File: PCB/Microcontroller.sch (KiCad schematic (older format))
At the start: 5 parts

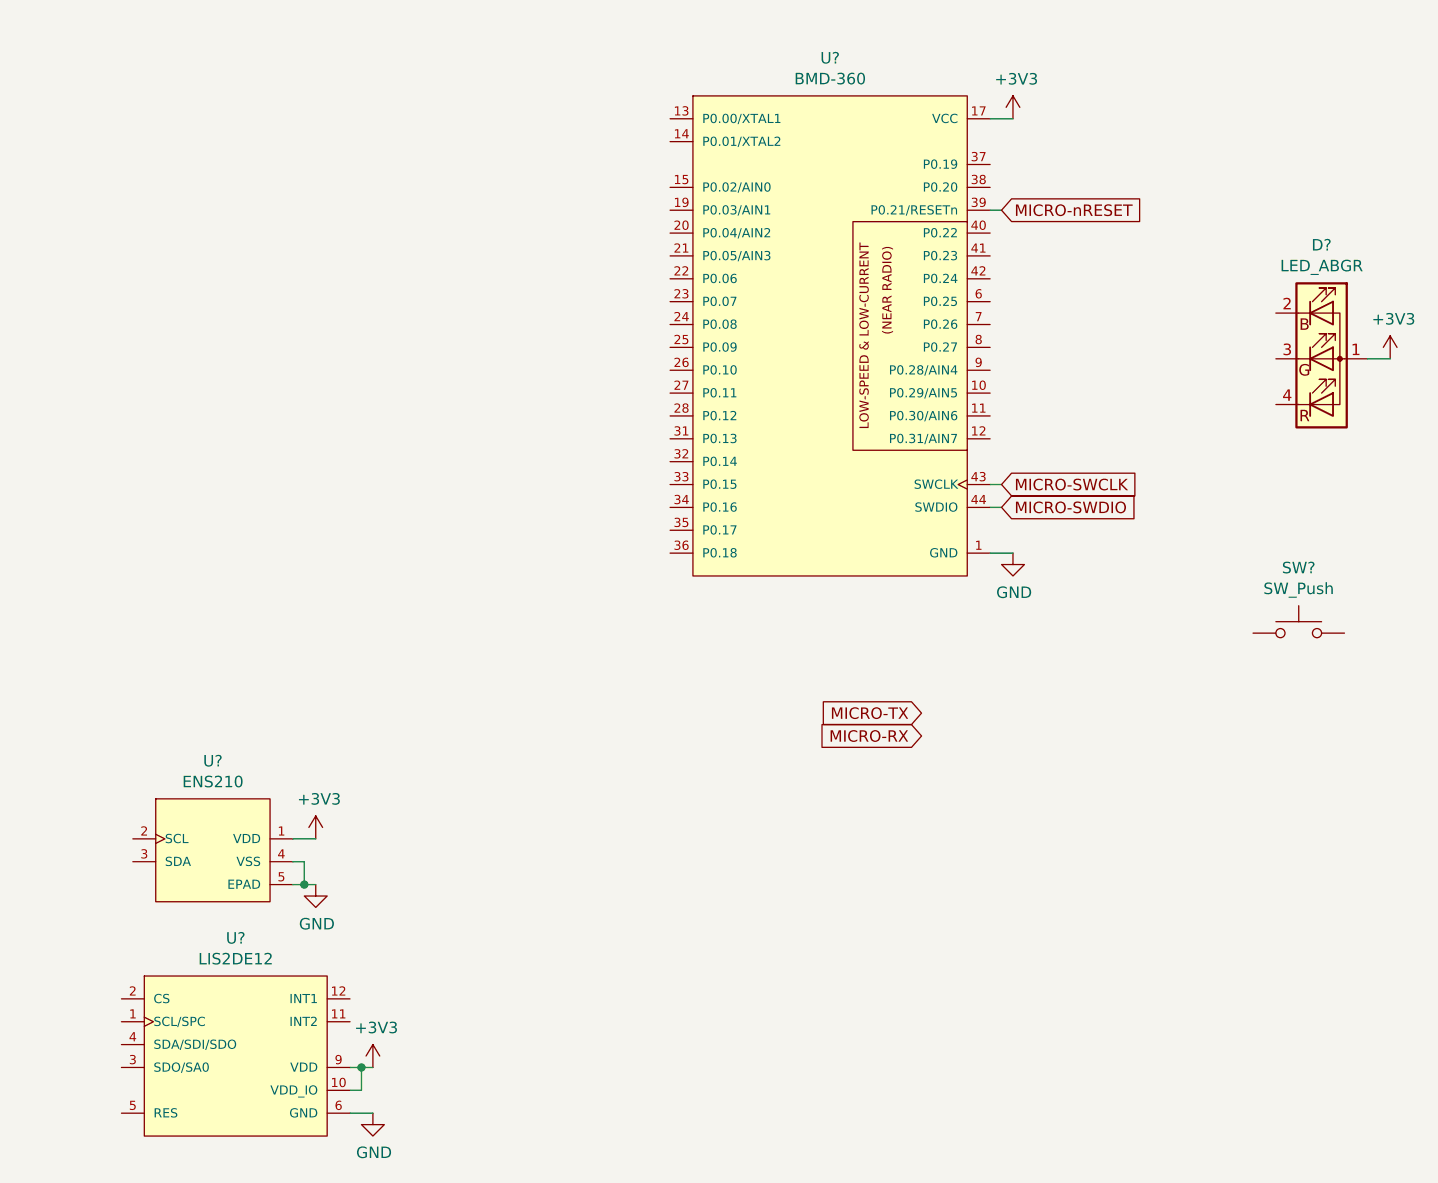
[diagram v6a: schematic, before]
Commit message: Add connections between FPGA and microcontroller
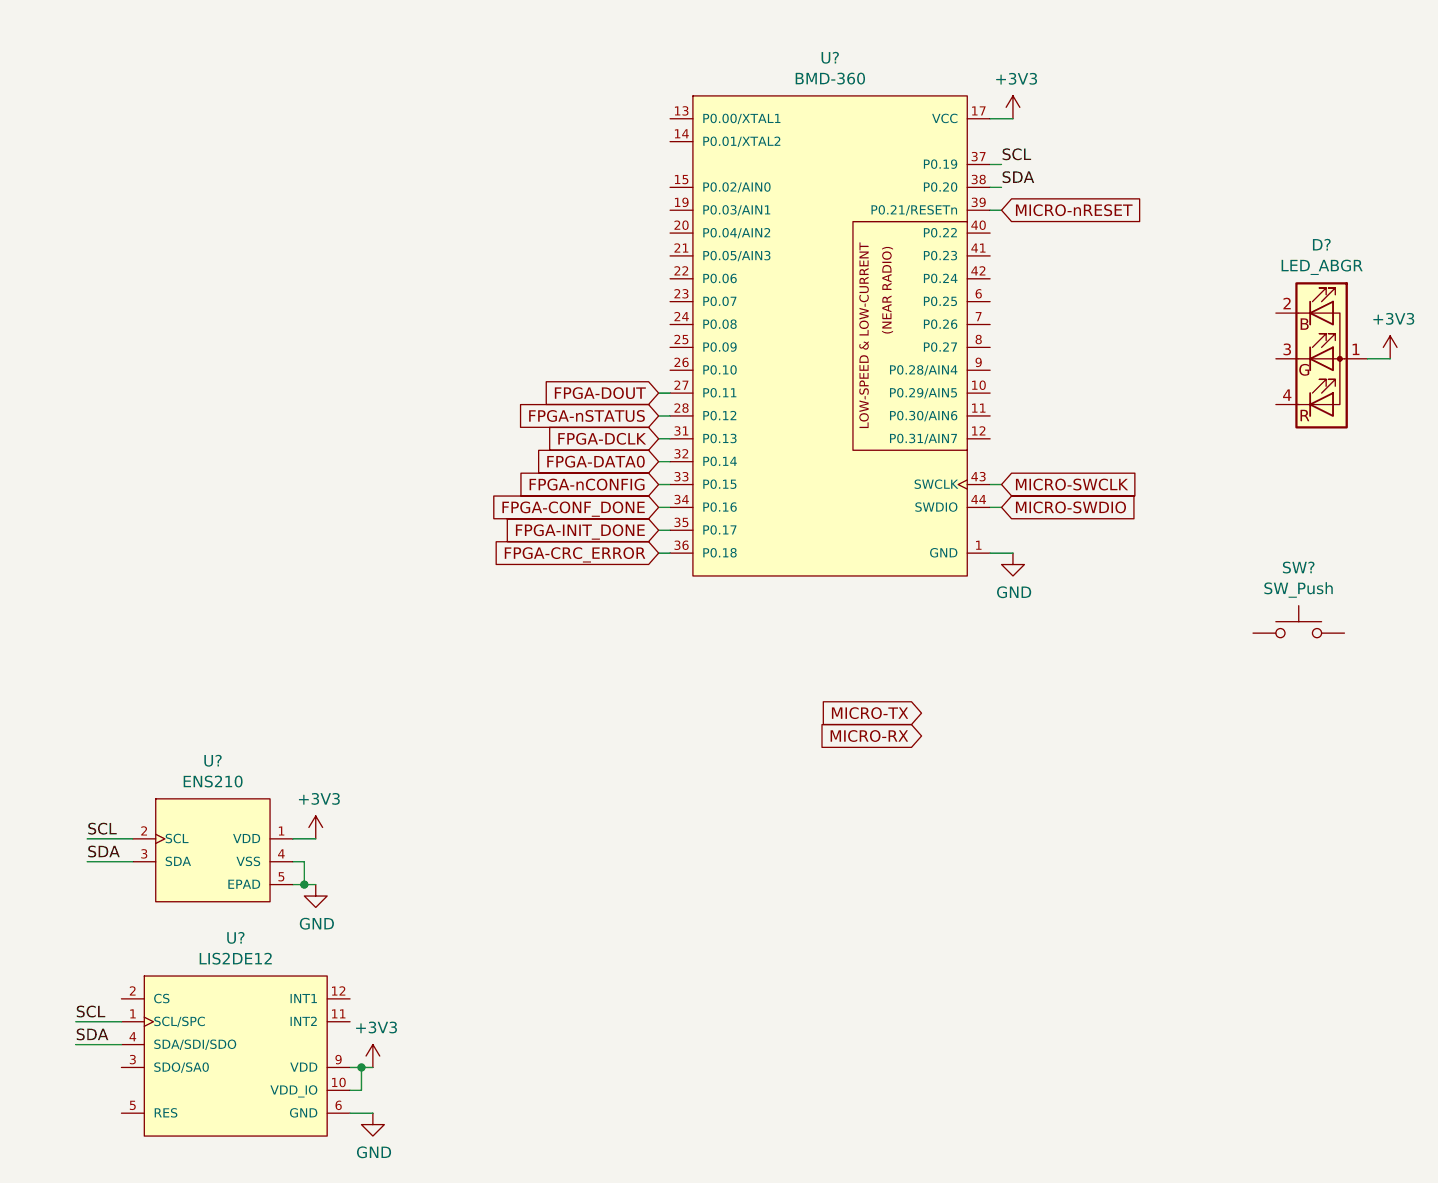
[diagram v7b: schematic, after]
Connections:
- net FPGA-DOUT: now reaches U?.27 (P0.11)
- net FPGA-nSTATUS: now reaches U?.28 (P0.12)
- net FPGA-DCLK: now reaches U?.31 (P0.13)
- net FPGA-DATA0: now reaches U?.32 (P0.14)
- net FPGA-nCONFIG: now reaches U?.33 (P0.15)
- net FPGA-CONF_DONE: now reaches U?.34 (P0.16)
- net FPGA-INIT_DONE: now reaches U?.35 (P0.17)
- net FPGA-CRC_ERROR: now reaches U?.36 (P0.18)
- net SCL: now reaches U?.37 (P0.19)
- net SCL: now also U?.1 (SCL/SPC), U?.2 (SCL)
- net SDA: now reaches U?.38 (P0.20)
- net SDA: now also U?.3 (SDA), U?.4 (SDA/SDI/SDO)
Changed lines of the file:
@@
 Wire Wire Line
 	5950 2800 5900 2800
+Text GLabel 4450 3700 0    50   Input ~ 0
+FPGA-nSTATUS
+Text GLabel 4450 3800 0    50   Input ~ 0
+FPGA-DCLK
+Text GLabel 4450 3900 0    50   Input ~ 0
+FPGA-DATA0
+Text GLabel 4450 4000 0    50   Input ~ 0
+FPGA-nCONFIG
+Text GLabel 4450 4100 0    50   Input ~ 0
+FPGA-CONF_DONE
+Text GLabel 4450 4200 0    50   Input ~ 0
+FPGA-INIT_DONE
+Text GLabel 4450 4300 0    50   Input ~ 0
+FPGA-CRC_ERROR
+Text Label 1950 5550 0    50   ~ 0
+SCL
+Text Label 1950 5650 0    50   ~ 0
+SDA
+Text Label 1900 6350 0    50   ~ 0
+SCL
+Text Label 1900 6450 0    50   ~ 0
+SDA
+Wire Wire Line
+	1950 5550 2150 5550
+Wire Wire Line
+	2150 5650 1950 5650
+Wire Wire Line
+	2100 6350 1900 6350
+Wire Wire Line
+	1900 6450 2100 6450
+Text Label 5950 2600 0    50   ~ 0
+SCL
+Text Label 5950 2700 0    50   ~ 0
+SDA
+Wire Wire Line
+	5950 2600 5900 2600
+Wire Wire Line
+	5900 2700 5950 2700
+Wire Wire Line
+	4450 4300 4500 4300
+Wire Wire Line
+	4500 4200 4450 4200
+Wire Wire Line
+	4450 4100 4500 4100
+Wire Wire Line
+	4500 4000 4450 4000
+Wire Wire Line
+	4450 3900 4500 3900
+Wire Wire Line
+	4500 3800 4450 3800
+Wire Wire Line
+	4450 3700 4500 3700
+Text GLabel 4450 3600 0    50   Input ~ 0
+FPGA-DOUT
+Wire Wire Line
+	4450 3600 4500 3600
 $EndSCHEMATC

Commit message: Connect LED to microcontroller, add another debugging header
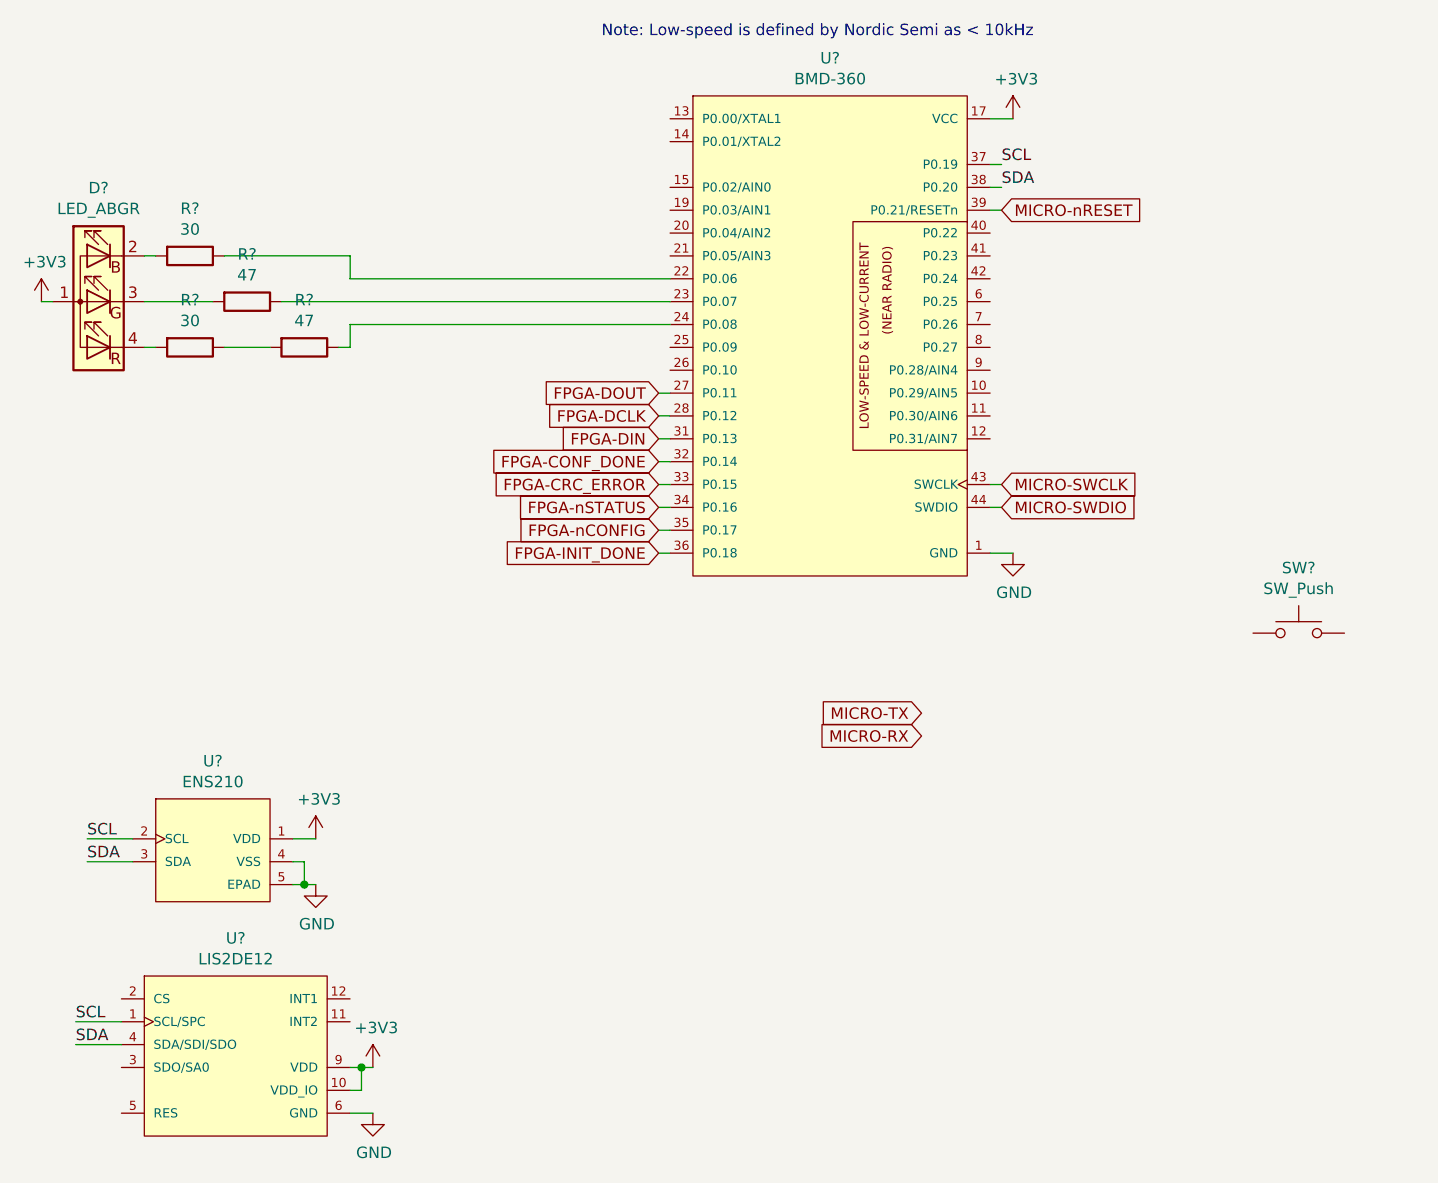
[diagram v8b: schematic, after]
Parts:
- added R? (x2): 47, Resistors_SMD:R_0603_HandSoldering, symbol Device:R
- added R? (x2): 30, Resistors_SMD:R_0603_HandSoldering, symbol Device:R
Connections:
- net FPGA-DATA0 is gone; now on net FPGA-CONF_DONE: U?.32 (P0.14)
- net FPGA-CONF_DONE: no longer U?.34 (P0.16)
- net FPGA-CRC_ERROR: now also U?.33 (P0.15); no longer U?.36 (P0.18)
- net FPGA-DCLK: now also U?.28 (P0.12); no longer U?.31 (P0.13)
- net FPGA-INIT_DONE: now also U?.36 (P0.18); no longer U?.35 (P0.17)
- net FPGA-nCONFIG: now also U?.35 (P0.17); no longer U?.33 (P0.15)
- net FPGA-nSTATUS: now also U?.34 (P0.16); no longer U?.28 (P0.12)
- net at U?.22 (P0.06): now also R?.1
- net at U?.23 (P0.07): now also R?.1
- net at U?.24 (P0.08): now also R?.1
- net at D?.2 (RK): now also R?.2
- net at D?.3 (GK): now also R?.2
- net at D?.4 (BK): now also R?.2
- new net: R?.1, R?.2
- new net FPGA-DIN: U?.31 (P0.13)
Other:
- note added: "Note: Low-speed is defined by Nordic Semi as < 10kHz"
- moved on the sheet: D?
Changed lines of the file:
@@
-$EndComp
-$Comp
-L Parts:LED_ABGR D?
-U 1 1 5DCF3816
-P 7350 3450
-F 0 "D?" H 7350 3947 50  0000 C CNN
-F 1 "LED_ABGR" H 7350 3856 50  0000 C CNN
-F 2 "Parts:CLMVC-FKA" H 7350 3025 50  0001 C CNN
-F 3 "https://www.cree.com/led-components/media/documents/1273-CLMVC-FKA.pdf" H 7350 3400 50  0001 C CNN
-	1    7350 3450
-	1    0    0    -1
 $EndComp
 $Comp
@@
 L power:+3V3 #PWR0127
 U 1 1 5DCF6F82
-P 7650 3450
-F 0 "#PWR0127" H 7650 3300 50  0001 C CNN
-F 1 "+3V3" H 7665 3623 50  0000 C CNN
-F 2 "" H 7650 3450 50  0001 C CNN
-F 3 "" H 7650 3450 50  0001 C CNN
-	1    7650 3450
-	1    0    0    -1
-$EndComp
-Wire Wire Line
-	7550 3450 7650 3450
+P 1750 3200
+F 0 "#PWR0127" H 1750 3050 50  0001 C CNN
+F 1 "+3V3" H 1765 3373 50  0000 C CNN
+F 2 "" H 1750 3200 50  0001 C CNN
+F 3 "" H 1750 3200 50  0001 C CNN
+	1    1750 3200
+	1    0    0    -1
+$EndComp
 $Comp
 L Parts:ENS210 U?
@@
 Wire Wire Line
 	5950 2800 5900 2800
+Text GLabel 4450 4100 0    50   Input ~ 0
+FPGA-nSTATUS
 Text GLabel 4450 3700 0    50   Input ~ 0
-FPGA-nSTATUS
+FPGA-DCLK
 Text GLabel 4450 3800 0    50   Input ~ 0
-FPGA-DCLK
+FPGA-DIN
+Text GLabel 4450 4200 0    50   Input ~ 0
+FPGA-nCONFIG
 Text GLabel 4450 3900 0    50   Input ~ 0
-FPGA-DATA0
+FPGA-CONF_DONE
+Text GLabel 4450 4300 0    50   Input ~ 0
+FPGA-INIT_DONE
 Text GLabel 4450 4000 0    50   Input ~ 0
-FPGA-nCONFIG
-Text GLabel 4450 4100 0    50   Input ~ 0
-FPGA-CONF_DONE
-Text GLabel 4450 4200 0    50   Input ~ 0
-FPGA-INIT_DONE
-Text GLabel 4450 4300 0    50   Input ~ 0
 FPGA-CRC_ERROR
 Text Label 1950 5550 0    50   ~ 0
@@
 Wire Wire Line
 	4450 3600 4500 3600
+Wire Wire Line
+	1750 3200 1800 3200
+Text Notes 4200 2050 0    50   ~ 0
+Note: Low-speed is defined by Nordic Semi as < 10kHz
+$Comp
+L Device:R R?
+U 1 1 5DF9D7B6
+P 2650 3200
+F 0 "R?" V 2443 3200 50  0000 C CNN
+F 1 "47" V 2534 3200 50  0000 C CNN
+F 2 "Resistors_SMD:R_0603_HandSoldering" V 2580 3200 50  0001 C CNN
+F 3 "https://www.digikey.ca/product-detail/en/stackpole-electronics-inc/RMCF0603FT47R0/RMCF0603FT47R0CT-ND/1942954" H 2650 3200 50  0001 C CNN
+	1    2650 3200
+	0    1    1    0
+$EndComp
+$Comp
+L Device:R R?
+U 1 1 5DF9DA34
+P 2400 3000
+F 0 "R?" V 2193 3000 50  0000 C CNN
+F 1 "30" V 2284 3000 50  0000 C CNN
+F 2 "Resistors_SMD:R_0603_HandSoldering" V 2330 3000 50  0001 C CNN
+F 3 "https://www.digikey.ca/product-detail/en/stackpole-electronics-inc/RMCF0603FT30R0/RMCF0603FT30R0CT-ND/4425092" H 2400 3000 50  0001 C CNN
+	1    2400 3000
+	0    1    1    0
+$EndComp
+$Comp
+L Parts:LED_ABGR D?
+U 1 1 5DCF3816
+P 2000 3200
+F 0 "D?" H 2000 3697 50  0000 C CNN
+F 1 "LED_ABGR" H 2000 3606 50  0000 C CNN
+F 2 "Parts:CLMVC-FKA" H 2000 2775 50  0001 C CNN
+F 3 "https://www.cree.com/led-components/media/documents/1273-CLMVC-FKA.pdf" H 2000 3150 50  0001 C CNN
+	1    2000 3200
+	-1   0    0    -1
+$EndComp
+Wire Wire Line
+	2200 3000 2250 3000
+Wire Wire Line
+	2200 3200 2500 3200
+Wire Wire Line
+	4500 3200 2800 3200
+Wire Wire Line
+	3050 3400 3100 3400
+Wire Wire Line
+	3100 3400 3100 3300
+Wire Wire Line
+	3100 3300 4500 3300
+Wire Wire Line
+	2550 3000 3100 3000
+Wire Wire Line
+	3100 3000 3100 3100
+Wire Wire Line
+	3100 3100 4500 3100
+$Comp
+L Device:R R?
+U 1 1 5DFB4959
+P 2400 3400
+F 0 "R?" V 2193 3400 50  0000 C CNN
+F 1 "30" V 2284 3400 50  0000 C CNN
+F 2 "Resistors_SMD:R_0603_HandSoldering" V 2330 3400 50  0001 C CNN
+F 3 "https://www.digikey.ca/product-detail/en/stackpole-electronics-inc/RMCF0603FT30R0/RMCF0603FT30R0CT-ND/4425092" H 2400 3400 50  0001 C CNN
+	1    2400 3400
+	0    1    1    0
+$EndComp
+$Comp
+L Device:R R?
+U 1 1 5DFB4DBC
+P 2900 3400
+F 0 "R?" V 2693 3400 50  0000 C CNN
+F 1 "47" V 2784 3400 50  0000 C CNN
+F 2 "Resistors_SMD:R_0603_HandSoldering" V 2830 3400 50  0001 C CNN
+F 3 "https://www.digikey.ca/product-detail/en/stackpole-electronics-inc/RMCF0603FT47R0/RMCF0603FT47R0CT-ND/1942954" H 2900 3400 50  0001 C CNN
+	1    2900 3400
+	0    1    1    0
+$EndComp
+Wire Wire Line
+	2550 3400 2750 3400
+Wire Wire Line
+	2250 3400 2200 3400
 $EndSCHEMATC
